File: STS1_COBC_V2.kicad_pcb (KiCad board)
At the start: 4 copper layers, 81 x 85 mm, 222 parts, among them IC2 STWD100PYW83F, IC3 STM32F411RET6TR, J1 UHF, J12 Conn_01x01_Male, J13 Conn_01x01_Male, J16 Conn_ARM_JTAG_SWD_10, J17 Conn_01x03_Male, J3 Conn_01x01_Male, J4 Conn_01x01_Male, J5 Conn_01x03_Male, J6 Conn_01x01_Male, J7 Conn_01x01_Male, J8 Conn_01x01_Male, J9 Conn_01x01_Male, Q1 SQ2318, Q2 BSS123, U1 coordinate_system, U10 TQP3M9036, U11 QPC1022, U12 FPF2701, U13 TQP7M9106, U14 MC14541BD, U15 MC74HC4538ADG, U2 LP2985-1.8, U3 MCP1725-3302E_MC, U4 74LVC2G74, U5 TYKTBCSANF-26.000000, U6 MP28167GQ, U7 NL17SV04XV5T2G, U8 Si4463, U9 LFCG-490+, Y1 Crystal_GND24

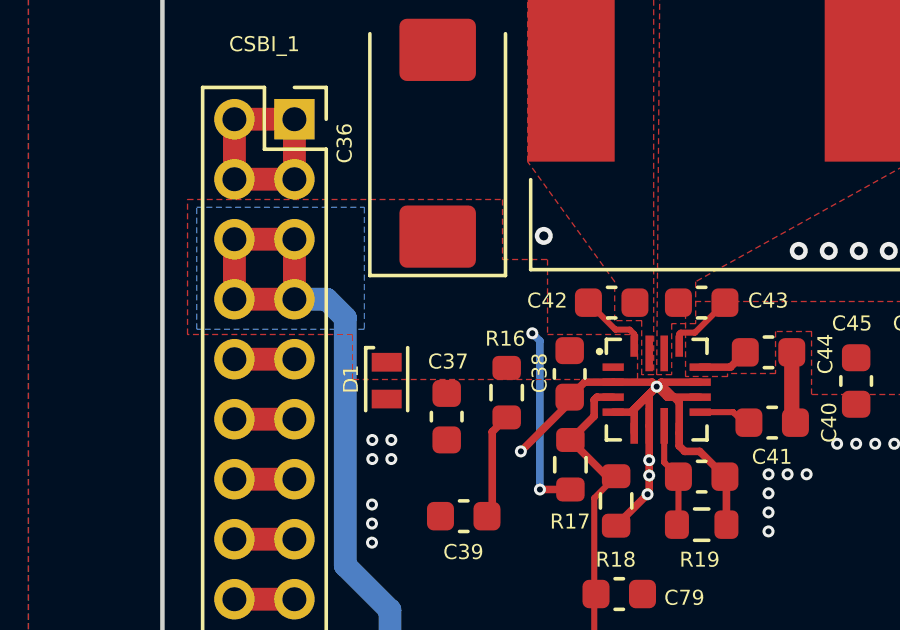
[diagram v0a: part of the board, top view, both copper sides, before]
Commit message: Add missing VBUS connection
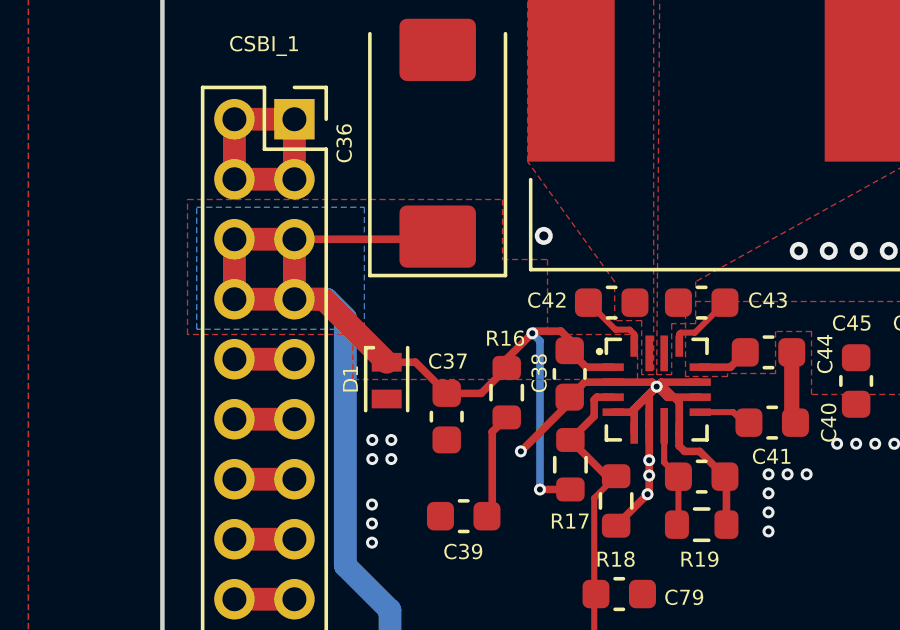
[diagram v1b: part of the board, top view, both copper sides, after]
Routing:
- net VBUS: track 167.2 -> 185.6 mm
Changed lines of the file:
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@@
   (segment (start 132.990344 96.40592) (end 128.800678 96.40592) (width 0.254) (layer "F.Cu") (net 8))
   (segment (start 128.800678 96.40592) (end 123.13254 102.074058) (width 0.254) (layer "F.Cu") (net 8))
+  (segment (start 125.575 73.4385) (end 126.725 73.4385) (width 0.254) (layer "F.Cu") (net 9))
+  (segment (start 131.125 72.563499) (end 130.224999 72.563499) (width 0.254) (layer "F.Cu") (net 9))
+  (segment (start 129.675 72.0135) (end 129.675 71.6543) (width 0.254) (layer "F.Cu") (net 9))
+  (segment (start 124.5375 72.401) (end 125.575 73.4385) (width 0.254) (layer "F.Cu") (net 9))
   (segment (start 120.5 68.3) (end 118.5 68.3) (width 0.762) (layer "F.Cu") (net 9))
   (segment (start 127.53254 118.55) (end 123.68254 114.7) (width 0.762) (layer "F.Cu") (net 9))
+  (segment (start 129.675 71.6543) (end 129.3842 71.3635) (width 0.254) (layer "F.Cu") (net 9))
   (segment (start 194.63254 106.3) (end 194.63254 108.3) (width 0.762) (layer "F.Cu") (net 9))
   (segment (start 129.699 76.6415) (end 128.684 76.6415) (width 0.254) (layer "F.Cu") (net 9))
@@
   (segment (start 131.68254 124.45) (end 127.53254 120.3) (width 0.762) (layer "F.Cu") (net 9))
   (segment (start 123.68254 108.8) (end 123.68254 107.66046) (width 0.762) (layer "F.Cu") (net 9))
+  (segment (start 120.5 70.3) (end 121.474 70.3) (width 0.762) (layer "F.Cu") (net 9))
+  (segment (start 126.725 73.4385) (end 127.575 72.5885) (width 0.254) (layer "F.Cu") (net 9))
+  (segment (start 123.575 72.401) (end 124.5375 72.401) (width 0.254) (layer "F.Cu") (net 9))
+  (segment (start 129.3842 71.3635) (end 128.501 71.3635) (width 0.254) (layer "F.Cu") (net 9))
   (segment (start 192.63254 108.3) (end 192.63254 106.3) (width 0.762) (layer "F.Cu") (net 9))
   (segment (start 118.5 70.3) (end 120.5 70.3) (width 0.762) (layer "F.Cu") (net 9))
+  (segment (start 121.474 70.3) (end 123.575 72.401) (width 0.762) (layer "F.Cu") (net 9))
   (segment (start 120.5 70.3) (end 120.5 68.3) (width 0.762) (layer "F.Cu") (net 9))
   (segment (start 127.53254 120.3) (end 127.53254 118.55) (width 0.762) (layer "F.Cu") (net 9))
+  (segment (start 127.575 72.5885) (end 127.575 72.2895) (width 0.254) (layer "F.Cu") (net 9))
+  (segment (start 127.575 72.2895) (end 128.429 71.4355) (width 0.254) (layer "F.Cu") (net 9))
   (segment (start 118.5 68.3) (end 118.5 70.3) (width 0.762) (layer "F.Cu") (net 9))
+  (segment (start 125.1875 68.3) (end 120.5 68.3) (width 0.254) (layer "F.Cu") (net 9))
   (segment (start 192.63254 106.3) (end 194.63254 106.3) (width 0.762) (layer "F.Cu") (net 9))
   (segment (start 194.63254 108.3) (end 192.63254 108.3) (width 0.762) (layer "F.Cu") (net 9))
+  (segment (start 125.275 68.2125) (end 125.1875 68.3) (width 0.254) (layer "F.Cu") (net 9))
   (segment (start 123.68254 114.7) (end 123.68254 108.8) (width 0.762) (layer "F.Cu") (net 9))
   (segment (start 128.684 76.6415) (end 128.683 76.6425) (width 0.254) (layer "F.Cu") (net 9))
+  (segment (start 128.501 71.3635) (end 128.429 71.4355) (width 0.254) (layer "F.Cu") (net 9))
+  (segment (start 130.224999 72.563499) (end 129.675 72.0135) (width 0.254) (layer "F.Cu") (net 9))
   (via (at 123.68254 108.16846) (size 0.4) (drill 0.2) (layers "F.Cu" "B.Cu") (net 9))
   (via (at 123.68254 107.66046) (size 0.4) (drill 0.2) (layers "F.Cu" "B.Cu") (net 9))

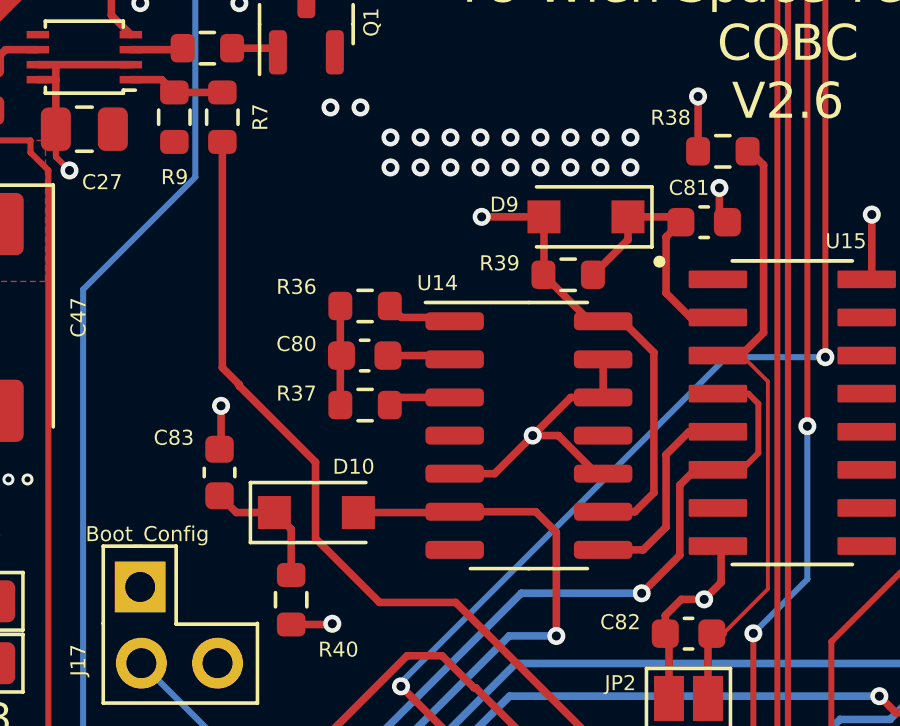
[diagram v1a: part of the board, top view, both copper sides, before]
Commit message: Replace schematics symbol of D9 and D10 diods
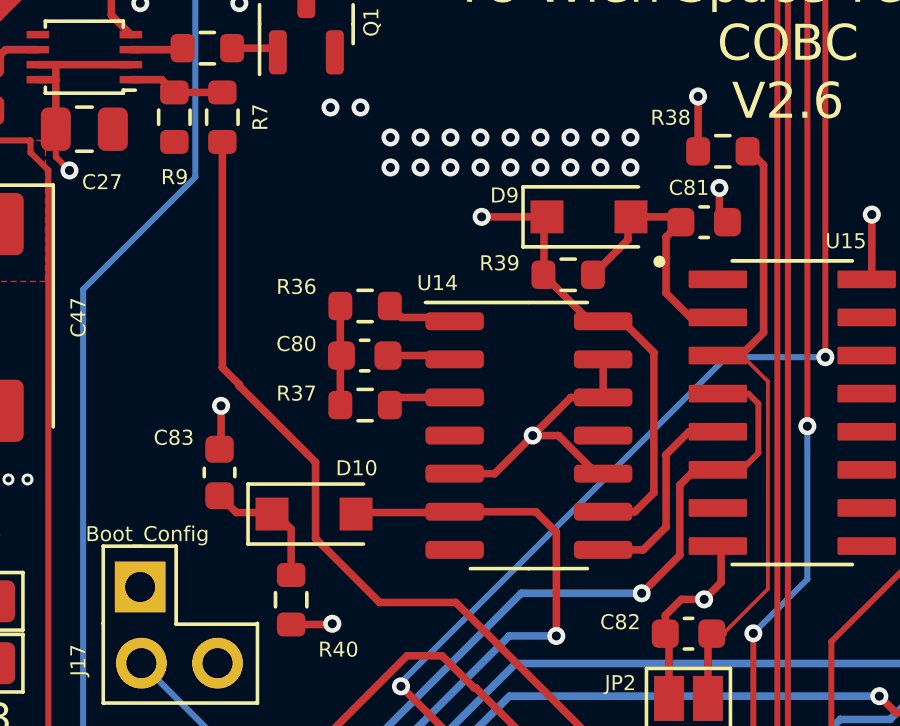
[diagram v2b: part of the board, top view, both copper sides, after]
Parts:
- moved D9 0.10 mm to (170.6, 75.1), turned to 0 degrees
- moved D10 0.09 mm to (161.4, 85.0)
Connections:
- D10 pad 1: Net-(C83-Pad2) -> /RDT_CLR
- D10 pad 2: /RDT_CLR -> Net-(C83-Pad2)
- D9 pad 1: Net-(C81-Pad1) -> +3V3
- D9 pad 2: +3V3 -> Net-(C81-Pad1)

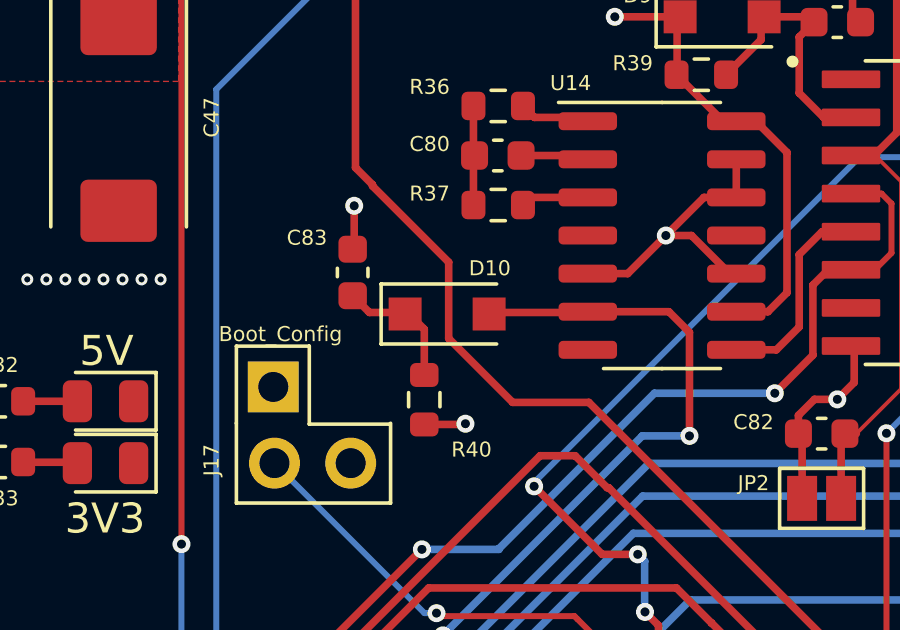
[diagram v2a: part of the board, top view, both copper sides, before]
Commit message: Flip D10 to correct orientation
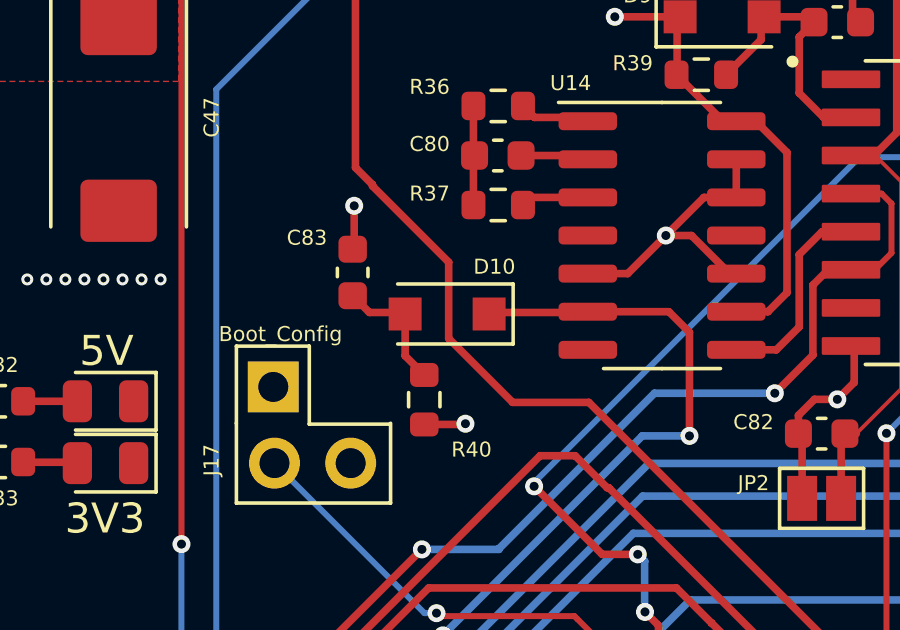
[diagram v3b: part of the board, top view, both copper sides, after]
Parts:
- turned D10 to 180 degrees
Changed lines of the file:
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@@
   )
   (footprint "Diode_SMD:D_SOD-123F" (layer "F.Cu")
-    (at 161.3882 85.0287)
+    (at 161.3882 85.0287 180)
     (descr "D_SOD-123F")
     (tags "D_SOD-123F")
@@
     (property "Sheetname" "Resetdog")
     (attr smd)
-    (fp_text reference "D10" (at 1.4224 -1.524) (layer "F.SilkS")
+    (fp_text reference "D10" (at -1.5748 1.5748) (layer "F.SilkS")
       (effects (font (size 0.5 0.5) (thickness 0.1)))
     )
-    (fp_text value "BAS70H" (at 1.1176 1.3716) (layer "F.Fab")
+    (fp_text value "BAS70H" (at -1.6764 -1.524) (layer "F.Fab")
       (effects (font (size 0.5 0.5) (thickness 0.1)))
     )
-    (fp_text user "${REFERENCE}" (at 1.4224 -1.524) (layer "F.Fab")
+    (fp_text user "${REFERENCE}" (at -1.5748 1.5748) (layer "F.Fab")
       (effects (font (size 0.5 0.5) (thickness 0.1)))
     )
@@
     (fp_line (start 0.25 0) (end 0.75 0) (layer "F.Fab") (width 0.1))
     (fp_line (start 0.25 0.4) (end -0.35 0) (layer "F.Fab") (width 0.1))
-    (pad "1" smd rect (at -1.4 0) (size 1.1 1.1) (layers "F.Cu" "F.Paste" "F.Mask")
+    (pad "1" smd rect (at -1.4 0 180) (size 1.1 1.1) (layers "F.Cu" "F.Paste" "F.Mask")
       (net 161 "/RDT_CLR") (pinfunction "K") (pintype "passive"))
-    (pad "2" smd rect (at 1.4 0) (size 1.1 1.1) (layers "F.Cu" "F.Paste" "F.Mask")
+    (pad "2" smd rect (at 1.4 0 180) (size 1.1 1.1) (layers "F.Cu" "F.Paste" "F.Mask")
       (net 171 "Net-(C83-Pad2)") (pinfunction "A") (pintype "passive"))
     (model "${KICAD6_3DMODEL_DIR}/Diode_SMD.3dshapes/D_SOD-123F.wrl"
@@
   (segment (start 173.123 83.0475) (end 173.885 82.2855) (width 0.254) (layer "F.Cu") (net 162))
   (segment (start 172.361 86.2225) (end 173.123 85.4605) (width 0.254) (layer "F.Cu") (net 162))
-  (segment (start 160.6262 87.0607) (end 160.6262 85.5367) (width 0.254) (layer "F.Cu") (net 171))
-  (segment (start 160.6262 85.5367) (end 160.0674 84.9779) (width 0.254) (layer "F.Cu") (net 171))
+  (segment (start 159.9882 85.0287) (end 159.9882 86.4227) (width 0.254) (layer "F.Cu") (net 171))
   (segment (start 158.7974 84.9779) (end 158.2386 84.4191) (width 0.254) (layer "F.Cu") (net 171))
+  (segment (start 159.9882 86.4227) (end 160.6262 87.0607) (width 0.254) (layer "F.Cu") (net 171))
   (segment (start 160.0674 84.9779) (end 158.7974 84.9779) (width 0.254) (layer "F.Cu") (net 171))
   (zone (net 9) (net_name "VBUS") (layer "F.Cu") (hatch edge 0.508)
